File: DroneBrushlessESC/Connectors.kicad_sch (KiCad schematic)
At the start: 0 parts

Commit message: Completed schematic for brushless ESC and added needed components to main board.  The plan is to mount the ESCs on the main board using 2.54mm Vert Conn Headers
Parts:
- added J1: UART, Connector_PinHeader_2.54mm:PinHeader_1x05_P2.54mm_Vertical, symbol Connector:Conn_01x05_Pin
- added J2: Screw_Terminal_01x03, Library:CUI_TB005_-762-03BE, symbol Connector:Screw_Terminal_01x03
- added J3: Debug, Connector_PinHeader_2.54mm:PinHeader_2x05_P2.54mm_Vertical, symbol Connector:Conn_01x10_Pin
- added J4: ~, Library:BrushlessESC, symbol Global:BrushlessESC
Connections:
- new net +3.3V: J1.2 (Pin_2), J3.1 (Pin_1), J4.1, J4.11
- new net FAULT_OUT: J4.9
- new net GND: J1.5 (Pin_5), J3.2 (Pin_2), J3.7 (Pin_7), J4.12, J4.2, J4.5, J4.8
- new net GNDPWR: J4.19, J4.20, J4.21, J4.22, J4.23, J4.24
- new net MTR_A: J2.3 (Pin_3)
- new net MTR_B: J2.2 (Pin_2)
- new net MTR_C: J2.1 (Pin_1)
- new net NRST_IN: J4.3
- new net PWM_IN: J4.6
- new net SWCLK: J3.4 (Pin_4)
- new net SWDIO: J3.3 (Pin_3)
- new net SWD_NRST: J3.5 (Pin_5)
- new net UART_RX: J1.4 (Pin_4)
- new net UART_TX: J1.3 (Pin_3)
- new net VDD: J4.13, J4.14, J4.15, J4.16, J4.17, J4.18
- no-connect marks 0 -> 8
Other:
- note added: "Debug/Prog Header"
- note added: "Motor Phase Outputs"
- note added: "UART Header"
- note added: "Vert Conn Mount"

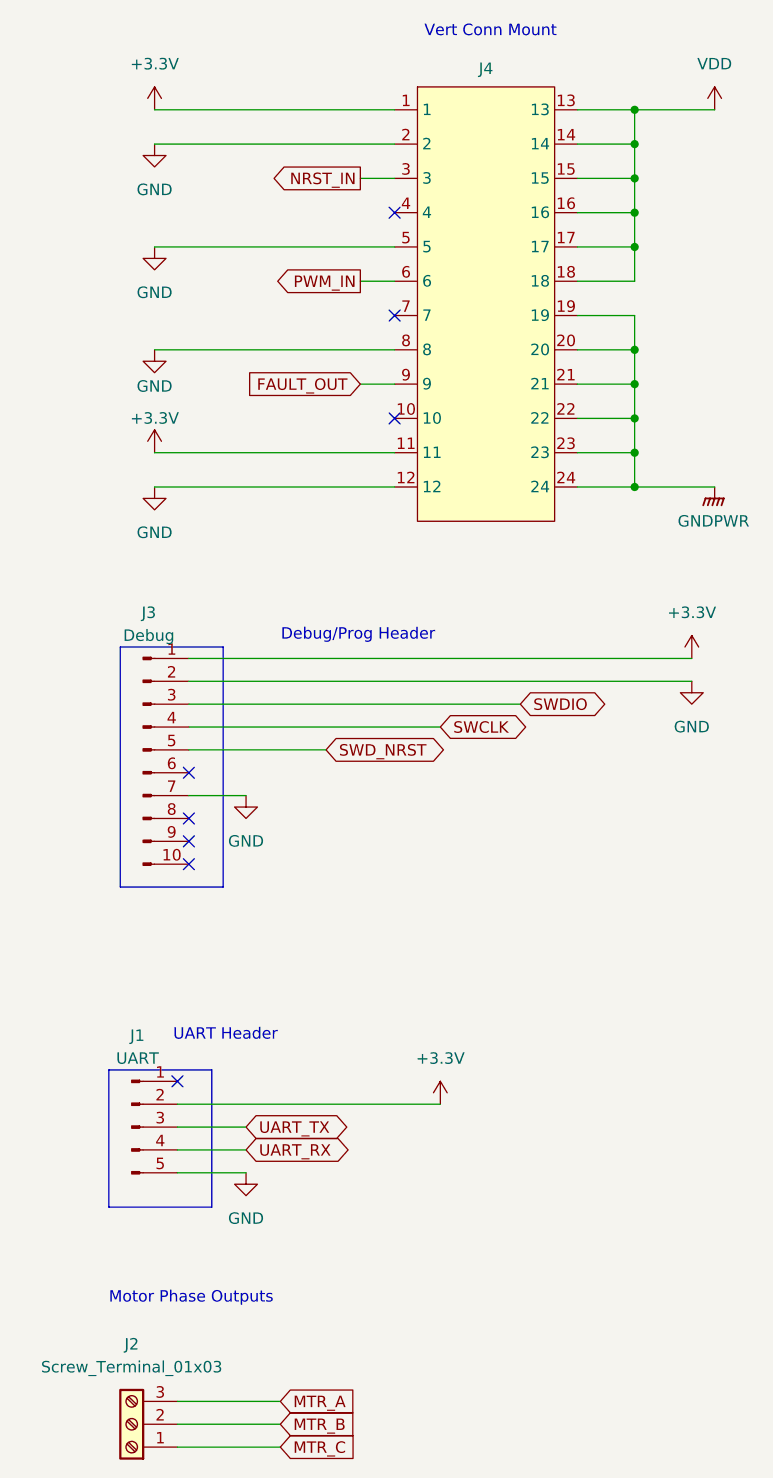
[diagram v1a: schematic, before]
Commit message: Finished layout for controller board
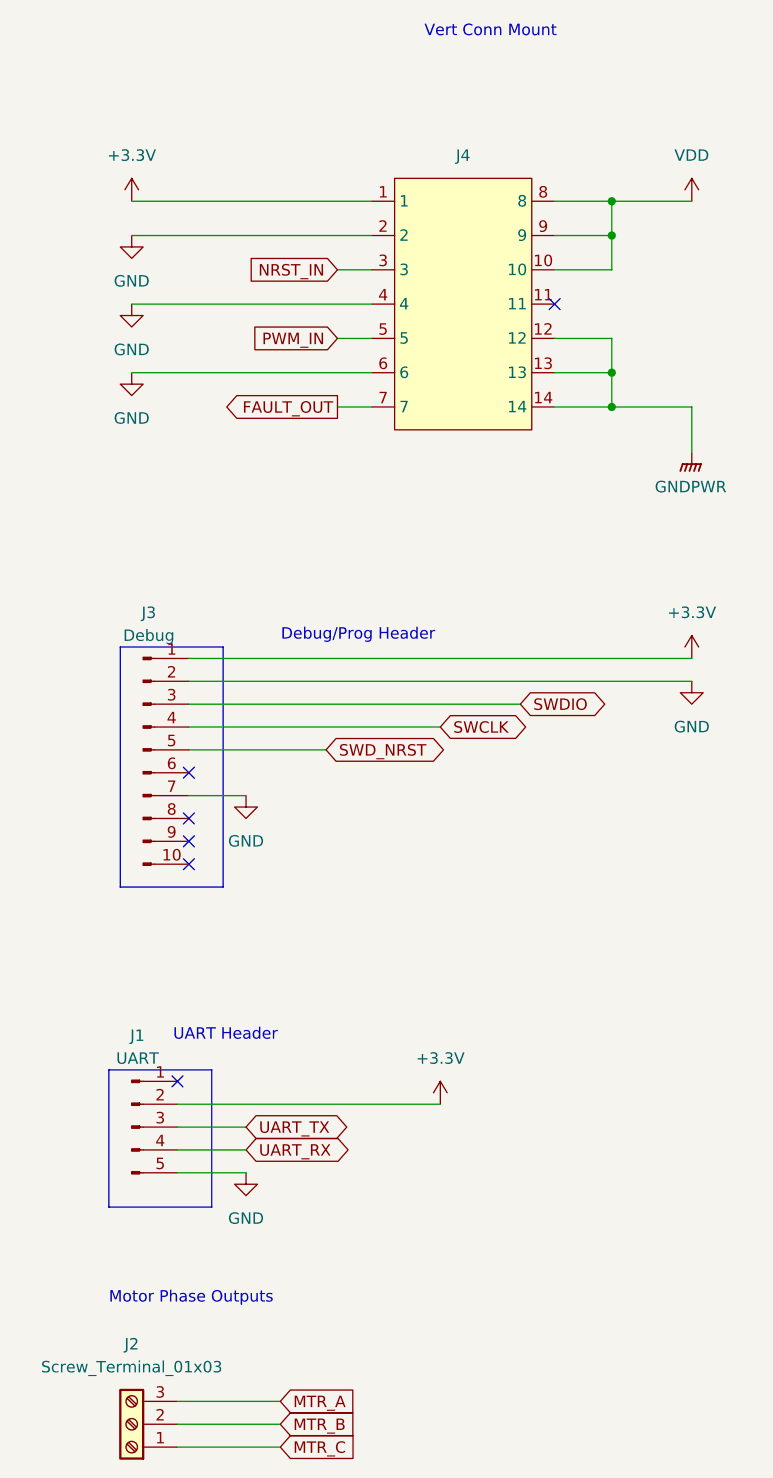
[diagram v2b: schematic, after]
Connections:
- net +3.3V: no longer J4.11
- net FAULT_OUT: now also J4.7; no longer J4.9
- net GND: now also J4.4, J4.6; no longer J4.12, J4.5, J4.8
- net GNDPWR: now also J4.12, J4.13, J4.14; no longer J4.19, J4.20, J4.21, J4.22, J4.23, J4.24
- net PWM_IN: now also J4.5; no longer J4.6
- net VDD: now also J4.10, J4.8, J4.9; no longer J4.13, J4.14, J4.15, J4.16, J4.17, J4.18
- no-connect marks 8 -> 6
